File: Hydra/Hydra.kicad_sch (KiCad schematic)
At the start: 72 parts, among them J1 USB_C_Receptacle_USB2.0, SW1 SW_Push, U1 USBLC6-2SC6, U2 ATmega32U4-M, Y1 16MHz

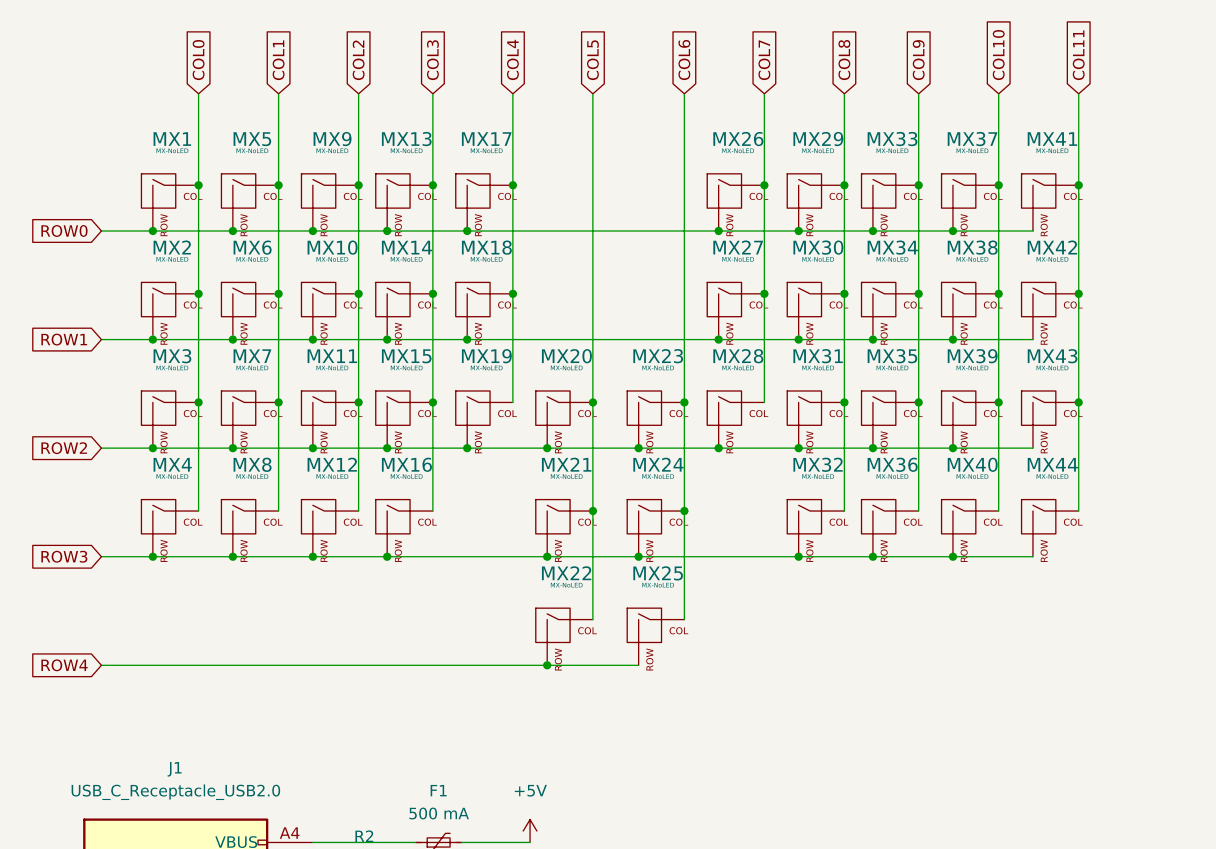
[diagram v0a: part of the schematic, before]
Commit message: Footprint assignment and placement of 50% switches
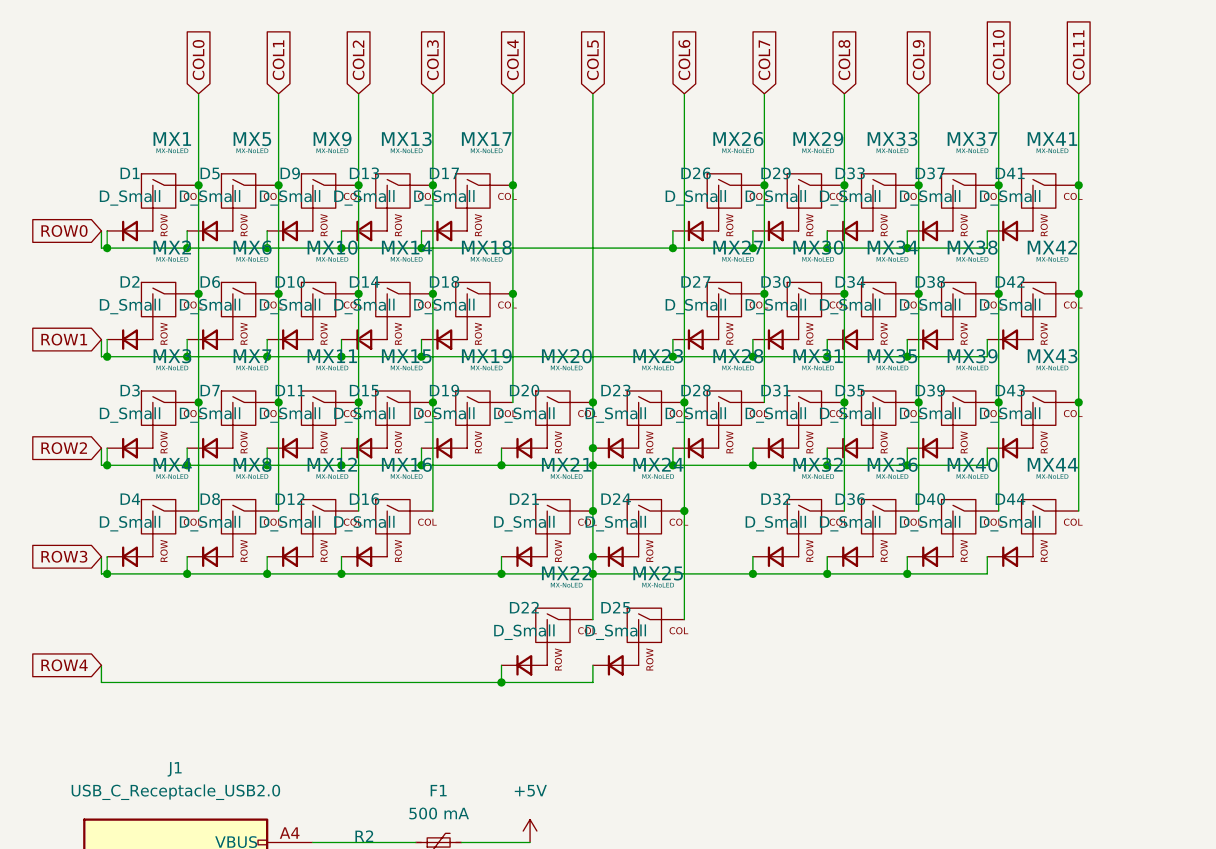
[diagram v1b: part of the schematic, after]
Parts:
- added D1, D10, D11, D12, D13, D14, D15, D16, D17, D18, D19, D2, D20, D21, D22, D23, D24, D25, D26, D27, D28, D29, D3, D30, D31, D32, D33, D34, D35, D36, D37, D38, D39, D4, D40, D41, D42, D43, D44, D5, D6, D7, D8, D9: D_Small, Diode_SMD:D_SOD-123, symbol Device:D_Small
- C1, C2, C3, C4, C5, C6, C7: footprint (none) -> Capacitor_SMD:C_0805_2012Metric
- F1: footprint (none) -> Fuse:Fuse_1206_3216Metric
- H1, H2, H3, H4, H5, H6, H7, H8: footprint (none) -> MountingHole:MountingHole_2.2mm_M2_Pad
- J1: footprint (none) -> USB_C_Receptacle_GT-USB-7010:USB_C_Receptacle_GT-USB-7010
- MX1, MX10, MX11, MX12, MX13, MX14, MX15, MX16, MX17, MX18, MX19, MX2, MX20, MX22, MX23, MX25, MX26, MX27, MX28, MX29, MX3, MX30, MX31, MX32, MX33, MX34, MX35, MX36, MX37, MX38, MX39, MX4, MX40, MX41, MX42, MX43, MX44, MX5, MX6, MX7, MX8, MX9: footprint (none) -> MX_Only:MXOnly-1U-NoLED
- MX21, MX24: footprint (none) -> MX_Only:MXOnly-2U-NoLED
- R1, R2, R3, R4, R5, R6, R7: footprint (none) -> Resistor_SMD:R_0805_2012Metric
- SW1: footprint (none) -> random-keyboard-parts:SKQG-1155865
- Y1: footprint (none) -> Crystal:Crystal_SMD_3225-4Pin_3.2x2.5mm
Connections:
- net COL5: now also D11.1 (K), D12.1 (K), D15.1 (K), D16.1 (K), D19.1 (K), D20.1 (K), D21.1 (K), D23.1 (K), D24.1 (K), D28.1 (K), D3.1 (K), D31.1 (K), D32.1 (K), D35.1 (K), D36.1 (K), D39.1 (K), D4.1 (K), D40.1 (K), D43.1 (K), D44.1 (K), D7.1 (K), D8.1 (K)
- net ROW0: now also D1.1 (K), D13.1 (K), D17.1 (K), D26.1 (K), D29.1 (K), D33.1 (K), D37.1 (K), D41.1 (K), D5.1 (K), D9.1 (K); no longer MX1.2 (ROW), MX13.2 (ROW), MX17.2 (ROW), MX26.2 (ROW), MX29.2 (ROW), MX33.2 (ROW), MX37.2 (ROW), MX41.2 (ROW), MX5.2 (ROW), MX9.2 (ROW)
- net ROW1: now also D10.1 (K), D14.1 (K), D18.1 (K), D2.1 (K), D27.1 (K), D30.1 (K), D34.1 (K), D38.1 (K), D42.1 (K), D6.1 (K); no longer MX10.2 (ROW), MX14.2 (ROW), MX18.2 (ROW), MX2.2 (ROW), MX27.2 (ROW), MX30.2 (ROW), MX34.2 (ROW), MX38.2 (ROW), MX42.2 (ROW), MX6.2 (ROW)
- net ROW4: now also D22.1 (K), D25.1 (K); no longer MX22.2 (ROW), MX25.2 (ROW)
- removed net ROW2: MX11.2 (ROW), MX15.2 (ROW), MX19.2 (ROW), MX20.2 (ROW), MX23.2 (ROW), MX28.2 (ROW), MX3.2 (ROW), MX31.2 (ROW), MX35.2 (ROW), MX39.2 (ROW), MX43.2 (ROW), MX7.2 (ROW)
- removed net ROW3: MX12.2 (ROW), MX16.2 (ROW), MX21.2 (ROW), MX24.2 (ROW), MX32.2 (ROW), MX36.2 (ROW), MX4.2 (ROW), MX40.2 (ROW), MX44.2 (ROW), MX8.2 (ROW)
- new net: D10.2 (A), MX10.2 (ROW)
- new net: D17.2 (A), MX17.2 (ROW)
- new net: D35.2 (A), MX35.2 (ROW)
- new net: D44.2 (A), MX44.2 (ROW)
- new net: D16.2 (A), MX16.2 (ROW)
- new net: D23.2 (A), MX23.2 (ROW)
- new net: D34.2 (A), MX34.2 (ROW)
- new net: D27.2 (A), MX27.2 (ROW)
- new net: D12.2 (A), MX12.2 (ROW)
- new net: D8.2 (A), MX8.2 (ROW)
- new net: D25.2 (A), MX25.2 (ROW)
- new net: D26.2 (A), MX26.2 (ROW)
- new net: D43.2 (A), MX43.2 (ROW)
- new net: D15.2 (A), MX15.2 (ROW)
- new net: D4.2 (A), MX4.2 (ROW)
- new net: D31.2 (A), MX31.2 (ROW)
- new net: D39.2 (A), MX39.2 (ROW)
- new net: D40.2 (A), MX40.2 (ROW)
- new net: D38.2 (A), MX38.2 (ROW)
- new net: D3.2 (A), MX3.2 (ROW)
- new net: D30.2 (A), MX30.2 (ROW)
- new net: D32.2 (A), MX32.2 (ROW)
- new net: D24.2 (A), MX24.2 (ROW)
- new net: D37.2 (A), MX37.2 (ROW)
- new net: D20.2 (A), MX20.2 (ROW)
- new net: D18.2 (A), MX18.2 (ROW)
- new net: D41.2 (A), MX41.2 (ROW)
- new net: D2.2 (A), MX2.2 (ROW)
- new net: D13.2 (A), MX13.2 (ROW)
- new net: D33.2 (A), MX33.2 (ROW)
- new net: D21.2 (A), MX21.2 (ROW)
- new net: D11.2 (A), MX11.2 (ROW)
- new net: D6.2 (A), MX6.2 (ROW)
- new net: D29.2 (A), MX29.2 (ROW)
- new net: D7.2 (A), MX7.2 (ROW)
- new net: D36.2 (A), MX36.2 (ROW)
- new net: D9.2 (A), MX9.2 (ROW)
- new net: D22.2 (A), MX22.2 (ROW)
- new net: D28.2 (A), MX28.2 (ROW)
- new net: D14.2 (A), MX14.2 (ROW)
- new net: D42.2 (A), MX42.2 (ROW)
- new net: D5.2 (A), MX5.2 (ROW)
- new net: D1.2 (A), MX1.2 (ROW)
- new net: D19.2 (A), MX19.2 (ROW)

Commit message: Fixed Schematic
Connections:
- net COL5: no longer D11.1 (K), D12.1 (K), D15.1 (K), D16.1 (K), D19.1 (K), D20.1 (K), D21.1 (K), D23.1 (K), D24.1 (K), D28.1 (K), D3.1 (K), D31.1 (K), D32.1 (K), D35.1 (K), D36.1 (K), D39.1 (K), D4.1 (K), D40.1 (K), D43.1 (K), D44.1 (K), D7.1 (K), D8.1 (K)
- new net ROW2: D11.1 (K), D15.1 (K), D19.1 (K), D20.1 (K), D23.1 (K), D28.1 (K), D3.1 (K), D31.1 (K), D35.1 (K), D39.1 (K), D43.1 (K), D7.1 (K)
- new net ROW3: D12.1 (K), D16.1 (K), D21.1 (K), D24.1 (K), D32.1 (K), D36.1 (K), D4.1 (K), D40.1 (K), D44.1 (K), D8.1 (K)
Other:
- moved on the sheet: D23, D24
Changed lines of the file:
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@@
   (junction (at 68.58 111.125) (diameter 0) (color 0 0 0 0)
   )
-  (junction (at 91.44 64.135) (diameter 0) (color 0 0 0 0)
-  )
   (junction (at 191.135 41.275) (diameter 0) (color 0 0 0 0)
   )
@@
   (junction (at 117.475 52.07) (diameter 0) (color 0 0 0 0)
   )
+  (junction (at 91.44 57.15) (diameter 0) (color 0 0 0 0)
+  )
   (junction (at 144.145 142.24) (diameter 0) (color 0 0 0 0)
   )
+  (junction (at 91.44 69.215) (diameter 0) (color 0 0 0 0)
+  )
   (junction (at 46.355 40.005) (diameter 0) (color 0 0 0 0)
   )
-  (junction (at 91.44 69.215) (diameter 0) (color 0 0 0 0)
-  )
   (junction (at 82.55 45.085) (diameter 0) (color 0 0 0 0)
   )
@@
   (junction (at 55.245 40.005) (diameter 0) (color 0 0 0 0)
   )
-  (junction (at 91.44 57.15) (diameter 0) (color 0 0 0 0)
-  )
   (junction (at 109.22 64.135) (diameter 0) (color 0 0 0 0)
   )
@@
   (junction (at 217.805 31.115) (diameter 0) (color 0 0 0 0)
   )
-  (junction (at 91.44 74.295) (diameter 0) (color 0 0 0 0)
+  (junction (at 90.805 76.2) (diameter 0) (color 0 0 0 0)
   )
   (junction (at 81.28 76.2) (diameter 0) (color 0 0 0 0)
@@
   (junction (at 101.6 57.15) (diameter 0) (color 0 0 0 0)
   )
-  (junction (at 91.44 62.23) (diameter 0) (color 0 0 0 0)
-  )
   (junction (at 126.365 64.135) (diameter 0) (color 0 0 0 0)
   )
-  (junction (at 91.44 76.2) (diameter 0) (color 0 0 0 0)
-  )
   (junction (at 65.405 45.085) (diameter 0) (color 0 0 0 0)
   )
@@
   )
   (junction (at 63.5 52.07) (diameter 0) (color 0 0 0 0)
+  )
+  (junction (at 90.805 64.135) (diameter 0) (color 0 0 0 0)
   )
   (junction (at 55.245 64.135) (diameter 0) (color 0 0 0 0)
@@
     (stroke (width 0) (type default) (color 0 0 0 0))
   )
-  (wire (pts (xy 91.44 74.295) (xy 91.44 76.2))
+  (wire (pts (xy 91.44 69.215) (xy 91.44 81.28))
     (stroke (width 0) (type default) (color 0 0 0 0))
   )
@@
     (stroke (width 0) (type default) (color 0 0 0 0))
   )
-  (wire (pts (xy 91.44 62.23) (xy 91.44 64.135))
-    (stroke (width 0) (type default) (color 0 0 0 0))
-  )
   (wire (pts (xy 123.825 142.24) (xy 137.16 142.24))
     (stroke (width 0) (type default) (color 0 0 0 0))
@@
     (stroke (width 0) (type default) (color 0 0 0 0))
   )
-  (wire (pts (xy 91.44 76.2) (xy 81.28 76.2))
-    (stroke (width 0) (type default) (color 0 0 0 0))
-  )
   (wire (pts (xy 60.325 113.665) (xy 63.5 113.665))
     (stroke (width 0) (type default) (color 0 0 0 0))
@@
     (stroke (width 0) (type default) (color 0 0 0 0))
   )
+  (wire (pts (xy 91.44 57.15) (xy 91.44 69.215))
+    (stroke (width 0) (type default) (color 0 0 0 0))
+  )
   (wire (pts (xy 82.55 45.085) (xy 82.55 57.15))
     (stroke (width 0) (type default) (color 0 0 0 0))
@@
     (stroke (width 0) (type default) (color 0 0 0 0))
   )
+  (wire (pts (xy 90.805 62.23) (xy 90.805 64.135))
+    (stroke (width 0) (type default) (color 0 0 0 0))
+  )
   (wire (pts (xy 37.465 50.165) (xy 37.465 52.07))
     (stroke (width 0) (type default) (color 0 0 0 0))
@@
     (stroke (width 0) (type default) (color 0 0 0 0))
   )
-  (wire (pts (xy 91.44 57.15) (xy 91.44 62.23))
-    (stroke (width 0) (type default) (color 0 0 0 0))
-  )
   (wire (pts (xy 101.6 22.86) (xy 101.6 57.15))
     (stroke (width 0) (type default) (color 0 0 0 0))
@@
     (stroke (width 0) (type default) (color 0 0 0 0))
   )
+  (wire (pts (xy 95.885 62.23) (xy 96.52 62.23))
+    (stroke (width 0) (type default) (color 0 0 0 0))
+  )
   (wire (pts (xy 37.465 52.07) (xy 36.83 52.07))
     (stroke (width 0) (type default) (color 0 0 0 0))
   )
-  (wire (pts (xy 109.22 76.2) (xy 91.44 76.2))
+  (wire (pts (xy 81.28 76.2) (xy 90.805 76.2))
     (stroke (width 0) (type default) (color 0 0 0 0))
   )
@@
     (stroke (width 0) (type default) (color 0 0 0 0))
   )
-  (wire (pts (xy 91.44 76.2) (xy 91.44 81.28))
-    (stroke (width 0) (type default) (color 0 0 0 0))
-  )
   (wire (pts (xy 144.145 137.16) (xy 150.495 137.16))
     (stroke (width 0) (type default) (color 0 0 0 0))
@@
     (stroke (width 0) (type default) (color 0 0 0 0))
   )
+  (wire (pts (xy 90.805 76.2) (xy 109.22 76.2))
+    (stroke (width 0) (type default) (color 0 0 0 0))
+  )
   (wire (pts (xy 65.405 45.085) (xy 65.405 57.15))
     (stroke (width 0) (type default) (color 0 0 0 0))
@@
     (stroke (width 0) (type default) (color 0 0 0 0))
   )
-  (wire (pts (xy 91.44 64.135) (xy 81.28 64.135))
-    (stroke (width 0) (type default) (color 0 0 0 0))
-  )
   (wire (pts (xy 252.095 84.455) (xy 256.54 84.455))
     (stroke (width 0) (type default) (color 0 0 0 0))
@@
     (stroke (width 0) (type default) (color 0 0 0 0))
   )
+  (wire (pts (xy 95.885 74.295) (xy 96.52 74.295))
+    (stroke (width 0) (type default) (color 0 0 0 0))
+  )
   (wire (pts (xy 127.635 45.085) (xy 127.635 57.15))
     (stroke (width 0) (type default) (color 0 0 0 0))
@@
     (stroke (width 0) (type default) (color 0 0 0 0))
   )
-  (wire (pts (xy 100.33 64.135) (xy 91.44 64.135))
+  (wire (pts (xy 81.28 64.135) (xy 90.805 64.135))
     (stroke (width 0) (type default) (color 0 0 0 0))
   )
@@
     (stroke (width 0) (type default) (color 0 0 0 0))
   )
-  (wire (pts (xy 91.44 69.215) (xy 91.44 74.295))
-    (stroke (width 0) (type default) (color 0 0 0 0))
-  )
   (wire (pts (xy 36.83 76.2) (xy 36.83 74.295))
     (stroke (width 0) (type default) (color 0 0 0 0))
@@
     (stroke (width 0) (type default) (color 0 0 0 0))
   )
+  (wire (pts (xy 90.805 64.135) (xy 100.33 64.135))
+    (stroke (width 0) (type default) (color 0 0 0 0))
+  )
   (wire (pts (xy 203.2 31.115) (xy 205.74 31.115))
     (stroke (width 0) (type default) (color 0 0 0 0))
@@
     (stroke (width 0) (type default) (color 0 0 0 0))
   )
+  (wire (pts (xy 90.805 74.295) (xy 90.805 76.2))
+    (stroke (width 0) (type default) (color 0 0 0 0))
+  )
   (wire (pts (xy 100.33 38.1) (xy 100.33 40.005))
     (stroke (width 0) (type default) (color 0 0 0 0))
@@
   )
   (wire (pts (xy 135.255 64.135) (xy 126.365 64.135))
-    (stroke (width 0) (type default) (color 0 0 0 0))
-  )
-  (wire (pts (xy 91.44 64.135) (xy 91.44 69.215))
     (stroke (width 0) (type default) (color 0 0 0 0))
   )
@@
     (pin "1")
   )
-  (symbol (lib_id "Device:D_Small") (at 93.98 62.23 0) (unit 1)
-    (in_bom yes) (on_board yes) (fields_autoplaced)
-    (property "Reference" "D23" (id 0) (at 93.98 55.88 0))
-    (property "Value" "D_Small" (id 1) (at 93.98 58.42 0))
-    (property "Footprint" "Diode_SMD:D_SOD-123" (id 2) (at 93.98 62.23 90)
-      (effects (font (size 1.27 1.27)) hide)
-    )
-    (property "Datasheet" "~" (id 3) (at 93.98 62.23 90)
+  (symbol (lib_id "Device:D_Small") (at 93.345 62.23 0) (unit 1)
+    (in_bom yes) (on_board yes) (fields_autoplaced)
+    (property "Reference" "D23" (id 0) (at 93.345 55.88 0))
+    (property "Value" "D_Small" (id 1) (at 93.345 58.42 0))
+    (property "Footprint" "Diode_SMD:D_SOD-123" (id 2) (at 93.345 62.23 90)
+      (effects (font (size 1.27 1.27)) hide)
+    )
+    (property "Datasheet" "~" (id 3) (at 93.345 62.23 90)
       (effects (font (size 1.27 1.27)) hide)
     )
@@
     (pin "1")
   )
-  (symbol (lib_id "Device:D_Small") (at 93.98 74.295 0) (unit 1)
-    (in_bom yes) (on_board yes) (fields_autoplaced)
-    (property "Reference" "D24" (id 0) (at 93.98 67.945 0))
-    (property "Value" "D_Small" (id 1) (at 93.98 70.485 0))
-    (property "Footprint" "Diode_SMD:D_SOD-123" (id 2) (at 93.98 74.295 90)
-      (effects (font (size 1.27 1.27)) hide)
-    )
-    (property "Datasheet" "~" (id 3) (at 93.98 74.295 90)
-      (effects (font (size 1.27 1.27)) hide)
-    )
+  (symbol (lib_id "Device:D_Small") (at 93.345 74.295 0) (unit 1)
+    (in_bom yes) (on_board yes) (fields_autoplaced)
+    (property "Reference" "D24" (id 0) (at 93.345 67.945 0))
+    (property "Value" "D_Small" (id 1) (at 93.345 70.485 0))
+    (property "Footprint" "Diode_SMD:D_SOD-123" (id 2) (at 93.345 74.295 90)
+      (effects (font (size 1.27 1.27)) hide)
+    )
+    (property "Datasheet" "~" (id 3) (at 93.345 74.295 90)
+      (effects (font (size 1.27 1.27)) hide)
+    )

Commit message: Cheeky matrix optimization
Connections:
- net ROW4 is gone; now on net ROW1: D22.1 (K), D25.1 (K)
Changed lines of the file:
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@@
   (junction (at 82.55 45.085) (diameter 0) (color 0 0 0 0)
   )
+  (junction (at 80.01 52.07) (diameter 0) (color 0 0 0 0)
+  )
   (junction (at 63.5 40.005) (diameter 0) (color 0 0 0 0)
   )
@@
   (junction (at 73.66 45.085) (diameter 0) (color 0 0 0 0)
   )
+  (junction (at 236.855 19.05) (diameter 0) (color 0 0 0 0)
+  )
+  (junction (at 127.635 57.15) (diameter 0) (color 0 0 0 0)
+  )
+  (junction (at 47.625 45.085) (diameter 0) (color 0 0 0 0)
+  )
+  (junction (at 150.495 142.24) (diameter 0) (color 0 0 0 0)
+  )
+  (junction (at 65.405 33.02) (diameter 0) (color 0 0 0 0)
+  )
+  (junction (at 150.495 137.16) (diameter 0) (color 0 0 0 0)
+  )
+  (junction (at 56.515 33.02) (diameter 0) (color 0 0 0 0)
+  )
+  (junction (at 109.22 40.005) (diameter 0) (color 0 0 0 0)
+  )
+  (junction (at 126.365 76.2) (diameter 0) (color 0 0 0 0)
+  )
+  (junction (at 56.515 57.15) (diameter 0) (color 0 0 0 0)
+  )
+  (junction (at 110.49 45.085) (diameter 0) (color 0 0 0 0)
+  )
+  (junction (at 73.66 57.15) (diameter 0) (color 0 0 0 0)
+  )
+  (junction (at 72.39 52.07) (diameter 0) (color 0 0 0 0)
+  )
+  (junction (at 137.16 142.24) (diameter 0) (color 0 0 0 0)
+  )
+  (junction (at 82.55 33.02) (diameter 0) (color 0 0 0 0)
+  )
+  (junction (at 127.635 33.02) (diameter 0) (color 0 0 0 0)
+  )
+  (junction (at 109.22 76.2) (diameter 0) (color 0 0 0 0)
+  )
+  (junction (at 110.49 33.02) (diameter 0) (color 0 0 0 0)
+  )
+  (junction (at 47.625 57.15) (diameter 0) (color 0 0 0 0)
+  )
+  (junction (at 136.525 57.15) (diameter 0) (color 0 0 0 0)
+  )
+  (junction (at 37.465 52.07) (diameter 0) (color 0 0 0 0)
+  )
+  (junction (at 145.415 45.085) (diameter 0) (color 0 0 0 0)
+  )
   (junction (at 81.28 88.265) (diameter 0) (color 0 0 0 0)
-  )
-  (junction (at 236.855 19.05) (diameter 0) (color 0 0 0 0)
-  )
-  (junction (at 127.635 57.15) (diameter 0) (color 0 0 0 0)
-  )
-  (junction (at 47.625 45.085) (diameter 0) (color 0 0 0 0)
-  )
-  (junction (at 150.495 142.24) (diameter 0) (color 0 0 0 0)
-  )
-  (junction (at 65.405 33.02) (diameter 0) (color 0 0 0 0)
-  )
-  (junction (at 150.495 137.16) (diameter 0) (color 0 0 0 0)
-  )
-  (junction (at 56.515 33.02) (diameter 0) (color 0 0 0 0)
-  )
-  (junction (at 109.22 40.005) (diameter 0) (color 0 0 0 0)
-  )
-  (junction (at 126.365 76.2) (diameter 0) (color 0 0 0 0)
-  )
-  (junction (at 56.515 57.15) (diameter 0) (color 0 0 0 0)
-  )
-  (junction (at 110.49 45.085) (diameter 0) (color 0 0 0 0)
-  )
-  (junction (at 73.66 57.15) (diameter 0) (color 0 0 0 0)
-  )
-  (junction (at 72.39 52.07) (diameter 0) (color 0 0 0 0)
-  )
-  (junction (at 137.16 142.24) (diameter 0) (color 0 0 0 0)
-  )
-  (junction (at 82.55 33.02) (diameter 0) (color 0 0 0 0)
-  )
-  (junction (at 127.635 33.02) (diameter 0) (color 0 0 0 0)
-  )
-  (junction (at 109.22 76.2) (diameter 0) (color 0 0 0 0)
-  )
-  (junction (at 110.49 33.02) (diameter 0) (color 0 0 0 0)
-  )
-  (junction (at 47.625 57.15) (diameter 0) (color 0 0 0 0)
-  )
-  (junction (at 136.525 57.15) (diameter 0) (color 0 0 0 0)
-  )
-  (junction (at 37.465 52.07) (diameter 0) (color 0 0 0 0)
-  )
-  (junction (at 145.415 45.085) (diameter 0) (color 0 0 0 0)
   )
   (junction (at 72.39 40.005) (diameter 0) (color 0 0 0 0)
@@
     (stroke (width 0) (type default) (color 0 0 0 0))
   )
-  (wire (pts (xy 81.28 88.265) (xy 36.83 88.265))
-    (stroke (width 0) (type default) (color 0 0 0 0))
-  )
   (wire (pts (xy 109.22 74.295) (xy 109.22 76.2))
     (stroke (width 0) (type default) (color 0 0 0 0))
@@
     (stroke (width 0) (type default) (color 0 0 0 0))
   )
+  (wire (pts (xy 81.28 88.265) (xy 80.01 88.265))
+    (stroke (width 0) (type default) (color 0 0 0 0))
+  )
   (wire (pts (xy 137.16 137.16) (xy 144.145 137.16))
     (stroke (width 0) (type default) (color 0 0 0 0))
@@
     (stroke (width 0) (type default) (color 0 0 0 0))
   )
+  (wire (pts (xy 80.01 52.07) (xy 72.39 52.07))
+    (stroke (width 0) (type default) (color 0 0 0 0))
+  )
   (wire (pts (xy 37.465 52.07) (xy 36.83 52.07))
     (stroke (width 0) (type default) (color 0 0 0 0))
@@
     (stroke (width 0) (type default) (color 0 0 0 0))
   )
-  (wire (pts (xy 100.33 52.07) (xy 72.39 52.07))
+  (wire (pts (xy 100.33 52.07) (xy 80.01 52.07))
     (stroke (width 0) (type default) (color 0 0 0 0))
   )
@@
     (stroke (width 0) (type default) (color 0 0 0 0))
   )
-  (wire (pts (xy 36.83 88.265) (xy 36.83 86.36))
-    (stroke (width 0) (type default) (color 0 0 0 0))
-  )
   (wire (pts (xy 145.415 57.15) (xy 145.415 69.215))
     (stroke (width 0) (type default) (color 0 0 0 0))
   )
   (wire (pts (xy 117.475 62.23) (xy 117.475 64.135))
+    (stroke (width 0) (type default) (color 0 0 0 0))
+  )
+  (wire (pts (xy 80.01 52.07) (xy 80.01 88.265))
     (stroke (width 0) (type default) (color 0 0 0 0))
   )
@@
     )
   )
-  (global_label "ROW4" (shape input) (at 36.83 86.36 180) (fields_autoplaced)
-    (effects (font (size 1.27 1.27)) (justify right))
-    (property "Intersheet References" "${INTERSHEET_REFS}" (id 0) (at 29.1555 86.2806 0)
-      (effects (font (size 1.27 1.27)) (justify right) hide)
-    )
-  )

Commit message: Even more optimizations
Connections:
- net ROW1: now also D20.1 (K), D23.1 (K), D28.1 (K); no longer D22.1 (K), D25.1 (K)
- net ROW2: now also D21.1 (K), D24.1 (K); no longer D20.1 (K), D23.1 (K), D28.1 (K), D31.1 (K), D35.1 (K), D39.1 (K), D43.1 (K)
- net ROW3: now also D22.1 (K), D25.1 (K); no longer D21.1 (K), D24.1 (K), D32.1 (K), D36.1 (K), D40.1 (K), D44.1 (K)
- new net: D31.1 (K), D35.1 (K), D39.1 (K), D43.1 (K)
- new net: D32.1 (K), D36.1 (K), D40.1 (K), D44.1 (K)
